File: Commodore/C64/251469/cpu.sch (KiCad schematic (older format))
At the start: 3 parts, among them U27 74LS08, U7 6510

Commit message: wip
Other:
- note removed: "RDY"
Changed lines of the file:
@@
 	1    0    0    -1
 $EndComp
-Text Notes 2150 4400 0    50   ~ 0
+Text Notes 2200 4850 1    50   ~ 0
 CAEC
-Text Notes 2100 5300 0    50   ~ 0
-RDY
 Wire Wire Line
 	1400 5250 1600 5250

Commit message: Checked all board caps (except RF modulator) in BOM against Service Manual parts list, and added type, voltage ratings and tolerance information from parts list to them
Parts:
- C9: Type (none) -> Ceramic; Voltage Rating (none) -> 25V
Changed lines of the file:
@@
 EESchema Schematic File Version 4
 LIBS:C64B-cache
-EELAYER 29 0
+EELAYER 30 0
 EELAYER END
 $Descr A4 11693 8268
@@
 F 2 "" H 3000 1350 50  0001 C CNN
 F 3 "~" H 3000 1350 50  0001 C CNN
+F 4 "Ceramic" H 3000 1350 50  0001 C CNN "Type"
+F 5 "25V" H 3000 1350 50  0001 C CNN "Voltage Rating"
 	1    3000 1350
 	0    1    1    0

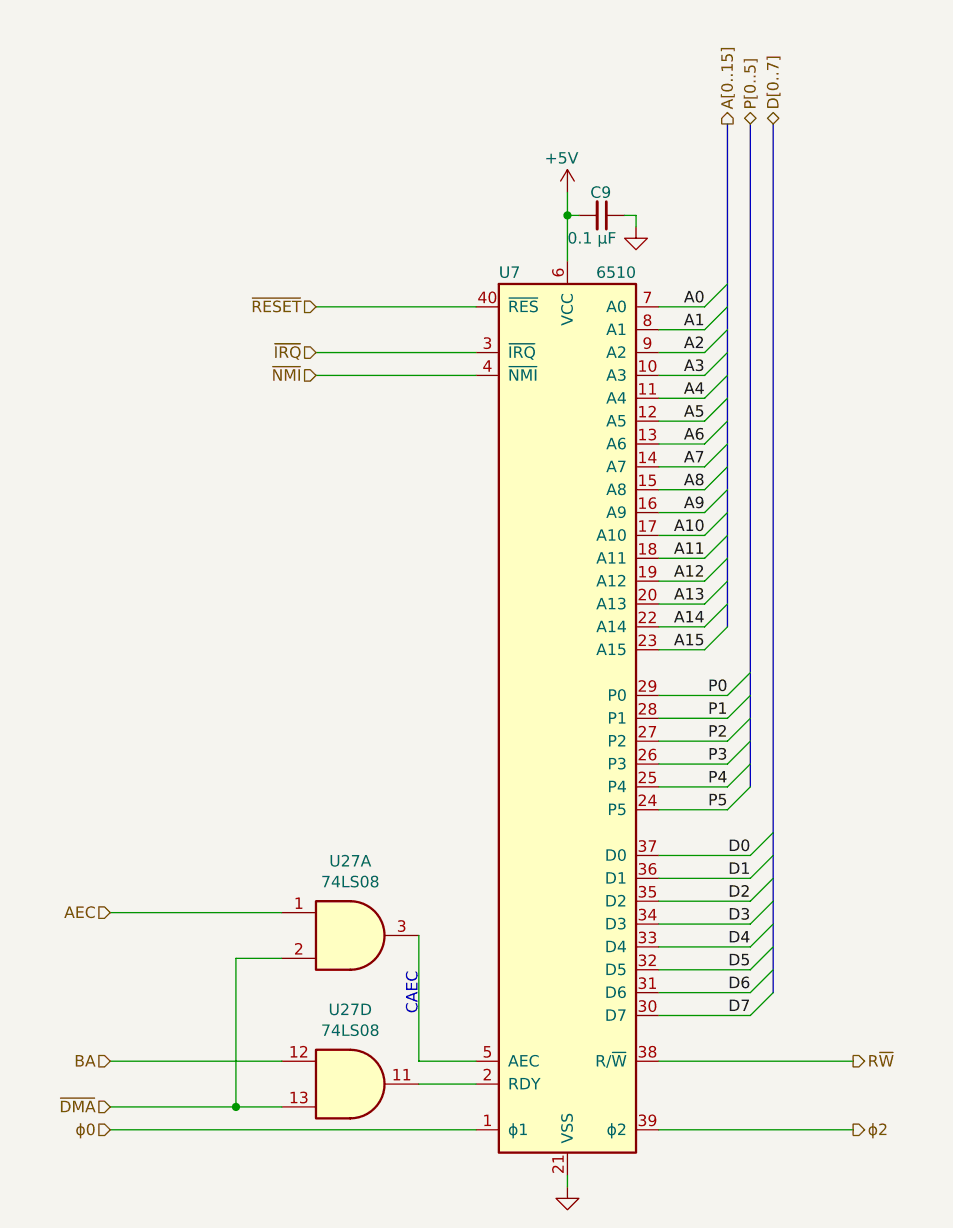
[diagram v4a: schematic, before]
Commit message: Added missing resistors R43, R44, R45 (pull-ups on /LORAM, /HIRAM and /CHAREN outputs from CPU P0-P2
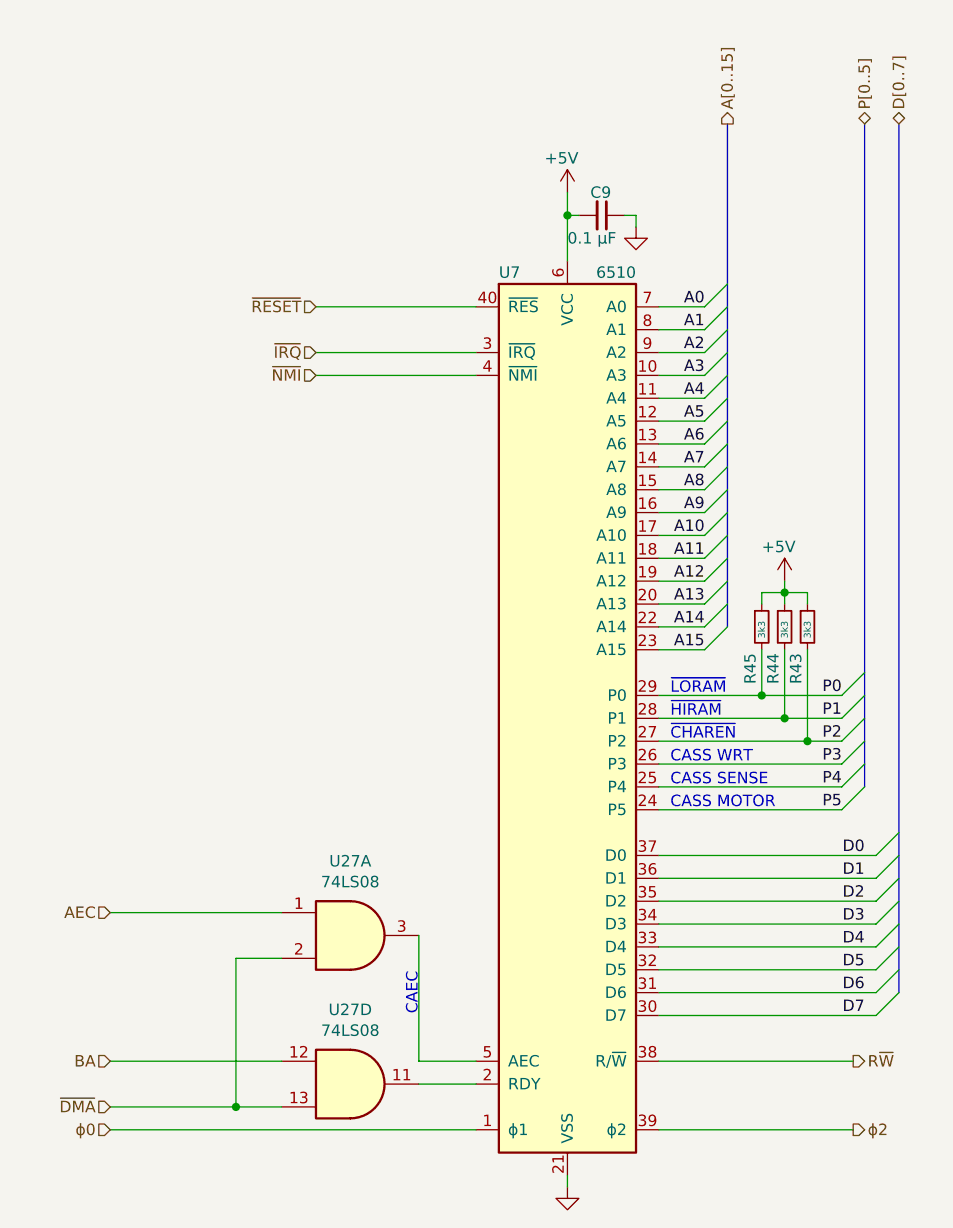
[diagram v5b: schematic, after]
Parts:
- added R43, R44, R45: 3k3, symbol Device:R_Small
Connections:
- net +5V: now also R43.1, R44.1, R45.1
- net P0: now also R45.2
- net P1: now also R44.2
- net P2: now also R43.2
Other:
- note added: "CASS MOTOR"
- note added: "CASS SENSE"
- note added: "CASS WRT"
- note added: "~CHAREN"
- note added: "~HIRAM"
- note added: "~LORAM"
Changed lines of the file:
@@
 EESchema Schematic File Version 4
 LIBS:C64B-cache
-EELAYER 30 0
+EELAYER 29 0
 EELAYER END
 $Descr A4 11693 8268
@@
 Text HLabel 3550 950  1    50   Output ~ 0
 A[0..15]
-Text HLabel 3750 950  1    50   BiDi ~ 0
+Text HLabel 4300 950  1    50   BiDi ~ 0
 D[0..7]
-Text HLabel 3650 950  1    50   BiDi ~ 0
+Text HLabel 4150 950  1    50   BiDi ~ 0
 P[0..5]
 Text HLabel 4100 5350 2    50   Output ~ 0
@@
 	3250 3250 3450 3250
 Wire Wire Line
-	3250 3450 3550 3450
-Wire Wire Line
-	3250 3550 3550 3550
-Wire Wire Line
-	3250 3650 3550 3650
-Wire Wire Line
-	3250 3750 3550 3750
-Wire Wire Line
-	3250 3850 3550 3850
-Wire Wire Line
-	3250 3950 3550 3950
-Wire Wire Line
-	3250 4150 3650 4150
-Wire Wire Line
-	3250 4850 3650 4850
-Wire Wire Line
-	3250 4750 3650 4750
-Wire Wire Line
-	3250 4650 3650 4650
-Wire Wire Line
-	3250 4550 3650 4550
-Wire Wire Line
-	3250 4450 3650 4450
-Wire Wire Line
-	3250 4350 3650 4350
-Wire Wire Line
-	3250 4250 3650 4250
-Text Label 3650 4850 2    50   ~ 0
+	3250 3450 3700 3450
+Text Label 4150 4850 2    50   ~ 0
 D7
-Text Label 3650 4750 2    50   ~ 0
+Text Label 4150 4750 2    50   ~ 0
 D6
-Text Label 3650 4650 2    50   ~ 0
+Text Label 4150 4650 2    50   ~ 0
 D5
-Text Label 3650 4550 2    50   ~ 0
+Text Label 4150 4550 2    50   ~ 0
 D4
-Text Label 3650 4450 2    50   ~ 0
+Text Label 4150 4450 2    50   ~ 0
 D3
-Text Label 3650 4350 2    50   ~ 0
+Text Label 4150 4350 2    50   ~ 0
 D2
-Text Label 3650 4250 2    50   ~ 0
+Text Label 4150 4250 2    50   ~ 0
 D1
-Text Label 3650 4150 2    50   ~ 0
+Text Label 4150 4150 2    50   ~ 0
 D0
 Entry Wire Line
-	3650 4150 3750 4050
-Entry Wire Line
-	3650 4250 3750 4150
-Entry Wire Line
-	3650 4850 3750 4750
-Entry Wire Line
-	3650 4750 3750 4650
-Entry Wire Line
-	3650 4650 3750 4550
-Entry Wire Line
-	3650 4550 3750 4450
-Entry Wire Line
-	3650 4450 3750 4350
-Entry Wire Line
-	3650 4350 3750 4250
-Text Label 3550 3950 2    50   ~ 0
+	4200 4150 4300 4050
+Entry Wire Line
+	4200 4250 4300 4150
+Entry Wire Line
+	4200 4850 4300 4750
+Entry Wire Line
+	4200 4750 4300 4650
+Entry Wire Line
+	4200 4650 4300 4550
+Entry Wire Line
+	4200 4550 4300 4450
+Entry Wire Line
+	4200 4450 4300 4350
+Entry Wire Line
+	4200 4350 4300 4250
+Text Label 4050 3950 2    50   ~ 0
 P5
-Text Label 3550 3850 2    50   ~ 0
+Text Label 4050 3850 2    50   ~ 0
 P4
-Text Label 3550 3750 2    50   ~ 0
+Text Label 4050 3750 2    50   ~ 0
 P3
-Text Label 3550 3650 2    50   ~ 0
+Text Label 4050 3650 2    50   ~ 0
 P2
-Text Label 3550 3550 2    50   ~ 0
+Text Label 4050 3550 2    50   ~ 0
 P1
-Text Label 3550 3450 2    50   ~ 0
+Text Label 4050 3450 2    50   ~ 0
 P0
 Entry Wire Line
-	3550 3450 3650 3350
-Entry Wire Line
-	3550 3550 3650 3450
-Entry Wire Line
-	3550 3650 3650 3550
-Entry Wire Line
-	3550 3750 3650 3650
-Entry Wire Line
-	3550 3850 3650 3750
-Entry Wire Line
-	3550 3950 3650 3850
+	4050 3450 4150 3350
+Entry Wire Line
+	4050 3550 4150 3450
+Entry Wire Line
+	4050 3650 4150 3550
+Entry Wire Line
+	4050 3750 4150 3650
+Entry Wire Line
+	4050 3850 4150 3750
+Entry Wire Line
+	4050 3950 4150 3850
 Wire Wire Line
 	2200 5150 2450 5150
@@
 Wire Wire Line
 	2850 5550 2850 5600
+$Comp
+L Device:R_Small R44
+U 1 1 5D4BF8F5
+P 3800 3150
+F 0 "R44" V 3750 2900 50  0000 L CNN
+F 1 "3k3" V 3800 3100 30  0000 L CNN
+F 2 "" H 3800 3150 50  0001 C CNN
+F 3 "~" H 3800 3150 50  0001 C CNN
+F 4 "5%" H 3800 3150 50  0001 C CNN "Ohmic Tolerance"
+F 5 "0.25 W" H 3800 3150 50  0001 C CNN "Power Rating"
+	1    3800 3150
+	1    0    0    -1
+$EndComp
+$Comp
+L power:+5V #PWR?
+U 1 1 5D4C0DC7
+P 3800 2950
+AR Path="/5D4C0DC7" Ref="#PWR?"  Part="1"
+AR Path="/5D28EBAC/5D4C0DC7" Ref="#PWR?"  Part="1"
+AR Path="/5D4AE438/5D4C0DC7" Ref="#PWR?"  Part="1"
+AR Path="/5D3AF8EC/5D4C0DC7" Ref="#PWR?"  Part="1"
+AR Path="/5D4581BB/5D4C0DC7" Ref="#PWR0261"  Part="1"
+F 0 "#PWR0261" H 3800 2800 50  0001 C CNN
+F 1 "+5V" H 3700 3100 50  0000 L CNN
+F 2 "" H 3800 2950 50  0001 C CNN
+F 3 "" H 3800 2950 50  0001 C CNN
+	1    3800 2950
+	1    0    0    -1
+$EndComp
+Wire Wire Line
+	3800 2950 3800 3000
+$Comp
+L Device:R_Small R43
+U 1 1 5D4C889C
+P 3900 3150
+F 0 "R43" V 3850 2900 50  0000 L CNN
+F 1 "3k3" V 3900 3100 30  0000 L CNN
+F 2 "" H 3900 3150 50  0001 C CNN
+F 3 "~" H 3900 3150 50  0001 C CNN
+F 4 "5%" H 3900 3150 50  0001 C CNN "Ohmic Tolerance"
+F 5 "0.25 W" H 3900 3150 50  0001 C CNN "Power Rating"
+	1    3900 3150
+	1    0    0    -1
+$EndComp
+$Comp
+L Device:R_Small R45
+U 1 1 5D4C8B57
+P 3700 3150
+F 0 "R45" V 3650 2900 50  0000 L CNN
+F 1 "3k3" V 3700 3100 30  0000 L CNN
+F 2 "" H 3700 3150 50  0001 C CNN
+F 3 "~" H 3700 3150 50  0001 C CNN
+F 4 "5%" H 3700 3150 50  0001 C CNN "Ohmic Tolerance"
+F 5 "0.25 W" H 3700 3150 50  0001 C CNN "Power Rating"
+	1    3700 3150
+	1    0    0    -1
+$EndComp
+Wire Wire Line
+	3700 3050 3700 3000
+Wire Wire Line
+	3700 3000 3800 3000
+Connection ~ 3800 3000
+Wire Wire Line
+	3800 3000 3800 3050
+Wire Wire Line
+	3800 3000 3900 3000
+Wire Wire Line
+	3900 3000 3900 3050
+Wire Wire Line
+	3250 3750 4050 3750
+Wire Wire Line
+	3250 3850 4050 3850
+Wire Wire Line
+	3250 3950 4050 3950
+Text Notes 3300 3450 0    50   ~ 0
+~LORAM
+Text Notes 3300 3550 0    50   ~ 0
+~HIRAM
+Text Notes 3300 3650 0    50   ~ 0
+~CHAREN
+Text Notes 3300 3750 0    50   ~ 0
+CASS WRT
+Text Notes 3300 3850 0    50   ~ 0
+CASS SENSE
+Text Notes 3300 3950 0    50   ~ 0
+CASS MOTOR
+Wire Wire Line
+	3700 3250 3700 3450
+Connection ~ 3700 3450
+Wire Wire Line
+	3700 3450 4050 3450
+Wire Wire Line
+	3800 3250 3800 3550
+Wire Wire Line
+	3250 3550 3800 3550
+Connection ~ 3800 3550
+Wire Wire Line
+	3800 3550 4050 3550
+Wire Wire Line
+	3900 3250 3900 3650
+Wire Wire Line
+	3250 3650 3900 3650
+Connection ~ 3900 3650
+Wire Wire Line
+	3900 3650 4050 3650
+Wire Wire Line
+	3250 4150 4200 4150
+Wire Wire Line
+	3250 4250 4200 4250
+Wire Wire Line
+	3250 4350 4200 4350
+Wire Wire Line
+	3250 4450 4200 4450
+Wire Wire Line
+	3250 4550 4200 4550
+Wire Wire Line
+	3250 4650 4200 4650
+Wire Wire Line
+	3250 4750 4200 4750
+Wire Wire Line
+	3250 4850 4200 4850
 Wire Bus Line
-	3650 950  3650 3850
+	4150 950  4150 3850
 Wire Bus Line
-	3750 950  3750 4750
+	4300 950  4300 4750
 Wire Bus Line
 	3550 950  3550 3150

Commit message: checked all diaodes (except in RF mod.) in KiCad schematic BOM against Service Manual parts list
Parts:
- R43, R44, R45: Power Rating 0.25 W -> 0.25W
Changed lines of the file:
@@
 F 3 "~" H 3800 3150 50  0001 C CNN
 F 4 "5%" H 3800 3150 50  0001 C CNN "Ohmic Tolerance"
-F 5 "0.25 W" H 3800 3150 50  0001 C CNN "Power Rating"
+F 5 "0.25W" H 3800 3150 50  0001 C CNN "Power Rating"
 	1    3800 3150
 	1    0    0    -1
@@
 F 3 "~" H 3900 3150 50  0001 C CNN
 F 4 "5%" H 3900 3150 50  0001 C CNN "Ohmic Tolerance"
-F 5 "0.25 W" H 3900 3150 50  0001 C CNN "Power Rating"
+F 5 "0.25W" H 3900 3150 50  0001 C CNN "Power Rating"
 	1    3900 3150
 	1    0    0    -1
@@
 F 3 "~" H 3700 3150 50  0001 C CNN
 F 4 "5%" H 3700 3150 50  0001 C CNN "Ohmic Tolerance"
-F 5 "0.25 W" H 3700 3150 50  0001 C CNN "Power Rating"
+F 5 "0.25W" H 3700 3150 50  0001 C CNN "Power Rating"
 	1    3700 3150
 	1    0    0    -1
